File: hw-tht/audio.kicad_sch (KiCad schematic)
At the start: 12 parts, among them U9 PCM5100A

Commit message: hw-tht: v1.3.0, axial/0805 hybrid resistors, decoupling placement
- Board revision v1.3.0 (schematic title blocks and README); take over
  the reviewed layout including the rotated PicoGUS logo and the new
  version and credit texts. The review board is now the build base, so
  its artwork is kept as drawn.
- New R_Axial_DIN0207_P10.16mm_0805_Hybrid footprint (0805 pads between
  the axial holes) for all resistors; BOM lists Yageo RC0805 (DigiKey)
  and UNI-ROYAL 0805W8F (LCSC) alternatives.
- Decoupling back next to the pins it serves, as on v1.2: DAC caps at
  CPVDD/CAPP-CAPM/VNEG/AVDD/DVDD, C4 at U2, C10 at the PSRAM, C3/C5 on
  the supply side of U3/U4. MIDI resistors and ferrites in one row
  next to J5, DAC output filters below the DAC.

Co-Authored-By: Claude Opus 5.5 <noreply@anthropic.com>
Claude-Session: https://claude.ai/code/session_011utN3x8yYUNDvkpGCEq5yD
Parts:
- R7, R8: footprint Resistor_THT:R_Axial_DIN0207_L6.3mm_D2.5mm_P10.16mm_Horizontal -> PicoGUS-THT:R_Axial_DIN0207_P10.16mm_0805_Hybrid; Alternatives (none) -> 0805 SMD (fits between the holes): Yageo RC0805FR-07470RL (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
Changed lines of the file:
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@@
 		(title "PicoGUS THT - PCM510x DAC")
 		(date "2026-09-28")
-		(rev "v1.2-THT")
+		(rev "v1.3.0")
 		(comment 1 "U9 stays SMD (TSSOP-20): PCM5100A/5101A/5102A only exist as SMD")
 	)
@@
 			)
 		)
-		(property "Footprint" "Resistor_THT:R_Axial_DIN0207_L6.3mm_D2.5mm_P10.16mm_Horizontal"
+		(property "Footprint" "PicoGUS-THT:R_Axial_DIN0207_P10.16mm_0805_Hybrid"
 			(at 80.01 48.26 0)
 			(hide yes)
@@
 		)
 		(property "LCSC" "C58592 (UNI-ROYAL MFR0W4F4700A50)"
+			(at 80.01 48.26 0)
+			(hide yes)
+			(effects
+				(font
+					(size 1.27 1.27)
+				)
+				(hide yes)
+			)
+		)
+		(property "Alternatives" "0805 SMD (fits between the holes): Yageo RC0805FR-07470RL (DK 311-470CRCT-ND, 109044), UNI-ROYAL 0805W8F (LCSC C17710, 2072700)."
 			(at 80.01 48.26 0)
 			(hide yes)
@@
 			)
 		)
-		(property "Footprint" "Resistor_THT:R_Axial_DIN0207_L6.3mm_D2.5mm_P10.16mm_Horizontal"
+		(property "Footprint" "PicoGUS-THT:R_Axial_DIN0207_P10.16mm_0805_Hybrid"
 			(at 80.01 45.72 0)
 			(hide yes)
@@
 			(at 80.01 45.72 0)
 			(hide yes)
+			(effects
+				(font
+					(size 1.27 1.27)
+				)
+				(hide yes)
+			)
+		)
+		(property "Alternatives" "0805 SMD (fits between the holes): Yageo RC0805FR-07470RL (DK 311-470CRCT-ND, 109044), UNI-ROYAL 0805W8F (LCSC C17710, 2072700)."
+			(at 80.01 45.72 0)
+			(hide yes)

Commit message: hw-tht: 5 mm disc/0805 hybrid capacitors, labels inside or beside bodies
- New C_Disc_D5.0mm_W2.5mm_P5.00mm_0805_Hybrid footprint for all ceramic
  caps: 5.0/5.08 mm radial part OR an 0805 between the holes. Replaces
  the 2.5/5.0 mm dual-pitch footprint.
- BOM: every ceramic cap line is now 5 mm pitch at both distributors
  (2.2 nF LCSC Dersonic C22391154, 100 pF DigiKey Vishay
  K101J15C0GF5TH5) and lists an in-stock 0805 alternative.
- Silkscreen labels: FB1/FB2 inside the body like the resistors;
  capacitor labels just outside the body, above/left, else at a free end.

Co-Authored-By: Claude Opus 5.5 <noreply@anthropic.com>
Claude-Session: https://claude.ai/code/session_011utN3x8yYUNDvkpGCEq5yD
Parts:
- C12, C13, C14, C18: footprint PicoGUS-THT:C_Disc_D5.0mm_W2.5mm_P2.50mm_P5.00mm -> PicoGUS-THT:C_Disc_D5.0mm_W2.5mm_P5.00mm_0805_Hybrid; Alternatives (none) -> 0805 SMD (fits between the holes): Samsung CL21B104KBCNNNC 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
- C15: footprint PicoGUS-THT:C_Disc_D5.0mm_W2.5mm_P2.50mm_P5.00mm -> PicoGUS-THT:C_Disc_D5.0mm_W2.5mm_P5.00mm_0805_Hybrid; Alternatives (none) -> 0805 SMD 25V X5R: Taiyo Yuden EMK212BJ106KG-T (DK 587-1295-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
- C16, C17: footprint PicoGUS-THT:C_Disc_D5.0mm_W2.5mm_P2.50mm_P5.00mm -> PicoGUS-THT:C_Disc_D5.0mm_W2.5mm_P5.00mm_0805_Hybrid; Alternatives 2.5 mm pitch FG14X7R1H225KRT06 (DK 445-173138-1-ND). -> 0805 SMD: Samsung CL21A225KAFNNNE 25V X5R (DK 1276-1763-1-N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
- C19, C20: footprint PicoGUS-THT:C_Disc_D5.0mm_W2.5mm_P2.50mm_P5.00mm -> PicoGUS-THT:C_Disc_D5.0mm_W2.5mm_P5.00mm_0805_Hybrid; Alternatives KEMET C320C222J1G5TA (DK 399-4281-ND), Vishay K222J15C0GF5T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 -> THT: Vishay K222J15C0GF5TH5 (DK BC1050CT-ND, 1744). 0805 SM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; LCSC C454405 (TORCH CC4-0805-CG-100V-2200pF-J-L (2.54 mm pitch)) -> C22391154 (Dersonic CD1H222JC9PECHD000 (5.08 mm pitch))
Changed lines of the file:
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@@
 			)
 		)
-		(property "Footprint" "PicoGUS-THT:C_Disc_D5.0mm_W2.5mm_P2.50mm_P5.00mm"
+		(property "Footprint" "PicoGUS-THT:C_Disc_D5.0mm_W2.5mm_P5.00mm_0805_Hybrid"
 			(at 90.805 50.8 0)
 			(hide yes)
@@
 			)
 		)
-		(property "LCSC" "C454405 (TORCH CC4-0805-CG-100V-2200pF-J-L (2.54 mm pitch))"
+		(property "LCSC" "C22391154 (Dersonic CD1H222JC9PECHD000 (5.08 mm pitch))"
 			(at 90.805 50.8 0)
 			(hide yes)
@@
 			)
 		)
-		(property "Alternatives" "KEMET C320C222J1G5TA (DK 399-4281-ND), Vishay K222J15C0GF5TL2 (DK BC1029CT-ND)."
+		(property "Alternatives" "THT: Vishay K222J15C0GF5TH5 (DK BC1050CT-ND, 1744). 0805 SMD: Yageo CC0805JRNPO9BN222 (DK 311-1103-1-ND, 126390) / CC0805JKNPO9BN222 (LCSC C107103, 165360)."
 			(at 90.805 50.8 0)
 			(hide yes)
@@
 			)
 		)
-		(property "Footprint" "PicoGUS-THT:C_Disc_D5.0mm_W2.5mm_P2.50mm_P5.00mm"
+		(property "Footprint" "PicoGUS-THT:C_Disc_D5.0mm_W2.5mm_P5.00mm_0805_Hybrid"
 			(at 22.86 47.625 0)
 			(hide yes)
@@
 		)
 		(property "LCSC" "C527620"
+			(at 22.86 47.625 0)
+			(hide yes)
+			(effects
+				(font
+					(size 1.27 1.27)
+				)
+				(hide yes)
+			)
+		)
+		(property "Alternatives" "0805 SMD (fits between the holes): Samsung CL21B104KBCNNNC (DK 1276-1003-1-ND, 4889645; LCSC C1711, 1029920)."
 			(at 22.86 47.625 0)
 			(hide yes)
@@
 			)
 		)
-		(property "Footprint" "PicoGUS-THT:C_Disc_D5.0mm_W2.5mm_P2.50mm_P5.00mm"
+		(property "Footprint" "PicoGUS-THT:C_Disc_D5.0mm_W2.5mm_P5.00mm_0805_Hybrid"
 			(at 80.01 66.04 0)
 			(hide yes)
@@
 		)
 		(property "LCSC" "C527620"
+			(at 80.01 66.04 0)
+			(hide yes)
+			(effects
+				(font
+					(size 1.27 1.27)
+				)
+				(hide yes)
+			)
+		)
+		(property "Alternatives" "0805 SMD (fits between the holes): Samsung CL21B104KBCNNNC (DK 1276-1003-1-ND, 4889645; LCSC C1711, 1029920)."
 			(at 80.01 66.04 0)
 			(hide yes)
@@
 			)
 		)
-		(property "Footprint" "PicoGUS-THT:C_Disc_D5.0mm_W2.5mm_P2.50mm_P5.00mm"
+		(property "Footprint" "PicoGUS-THT:C_Disc_D5.0mm_W2.5mm_P5.00mm_0805_Hybrid"
 			(at 77.47 57.15 0)
 			(hide yes)
@@
 			)
 		)
-		(property "Alternatives" "2.5 mm pitch FG14X7R1H225KRT06 (DK 445-173138-1-ND)."
+		(property "Alternatives" "0805 SMD: Samsung CL21A225KAFNNNE 25V X5R (DK 1276-1763-1-ND, 83806; LCSC C87994, 38740)."
 			(at 77.47 57.15 0)
 			(hide yes)
@@
 			)
 		)
-		(property "Footprint" "PicoGUS-THT:C_Disc_D5.0mm_W2.5mm_P2.50mm_P5.00mm"
+		(property "Footprint" "PicoGUS-THT:C_Disc_D5.0mm_W2.5mm_P5.00mm_0805_Hybrid"
 			(at 90.805 43.18 0)
 			(hide yes)
@@
 			)
 		)
-		(property "LCSC" "C454405 (TORCH CC4-0805-CG-100V-2200pF-J-L (2.54 mm pitch))"
+		(property "LCSC" "C22391154 (Dersonic CD1H222JC9PECHD000 (5.08 mm pitch))"
 			(at 90.805 43.18 0)
 			(hide yes)
@@
 			)
 		)
-		(property "Alternatives" "KEMET C320C222J1G5TA (DK 399-4281-ND), Vishay K222J15C0GF5TL2 (DK BC1029CT-ND)."
+		(property "Alternatives" "THT: Vishay K222J15C0GF5TH5 (DK BC1050CT-ND, 1744). 0805 SMD: Yageo CC0805JRNPO9BN222 (DK 311-1103-1-ND, 126390) / CC0805JKNPO9BN222 (LCSC C107103, 165360)."
 			(at 90.805 43.18 0)
 			(hide yes)
@@
 			)
 		)
-		(property "Footprint" "PicoGUS-THT:C_Disc_D5.0mm_W2.5mm_P2.50mm_P5.00mm"
+		(property "Footprint" "PicoGUS-THT:C_Disc_D5.0mm_W2.5mm_P5.00mm_0805_Hybrid"
 			(at 27.305 47.625 0)
 			(hide yes)
@@
 		)
 		(property "LCSC" "C527620"
+			(at 27.305 47.625 0)
+			(hide yes)
+			(effects
+				(font
+					(size 1.27 1.27)
+				)
+				(hide yes)
+			)
+		)
+		(property "Alternatives" "0805 SMD (fits between the holes): Samsung CL21B104KBCNNNC (DK 1276-1003-1-ND, 4889645; LCSC C1711, 1029920)."
 			(at 27.305 47.625 0)
 			(hide yes)
@@
 			)
 		)
-		(property "Footprint" "PicoGUS-THT:C_Disc_D5.0mm_W2.5mm_P2.50mm_P5.00mm"
+		(property "Footprint" "PicoGUS-THT:C_Disc_D5.0mm_W2.5mm_P5.00mm_0805_Hybrid"
 			(at 36.195 47.625 0)
 			(hide yes)
@@
 		)
 		(property "LCSC" "C3690252"
+			(at 36.195 47.625 0)
+			(hide yes)
+			(effects
+				(font
+					(size 1.27 1.27)
+				)
+				(hide yes)
+			)
+		)
+		(property "Alternatives" "0805 SMD 25V X5R: Taiyo Yuden EMK212BJ106KG-T (DK 587-1295-1-ND, 1864) or Samsung CL21A106KAYNNNE (LCSC C15850, 878060)."
 			(at 36.195 47.625 0)
 			(hide yes)
@@
 			)
 		)
-		(property "Footprint" "PicoGUS-THT:C_Disc_D5.0mm_W2.5mm_P2.50mm_P5.00mm"
+		(property "Footprint" "PicoGUS-THT:C_Disc_D5.0mm_W2.5mm_P5.00mm_0805_Hybrid"
 			(at 77.47 71.12 0)
 			(hide yes)
@@
 			)
 		)
-		(property "Alternatives" "2.5 mm pitch FG14X7R1H225KRT06 (DK 445-173138-1-ND)."
+		(property "Alternatives" "0805 SMD: Samsung CL21A225KAFNNNE 25V X5R (DK 1276-1763-1-ND, 83806; LCSC C87994, 38740)."
 			(at 77.47 71.12 0)
 			(hide yes)
@@
 			)
 		)
-		(property "Footprint" "PicoGUS-THT:C_Disc_D5.0mm_W2.5mm_P2.50mm_P5.00mm"
+		(property "Footprint" "PicoGUS-THT:C_Disc_D5.0mm_W2.5mm_P5.00mm_0805_Hybrid"
 			(at 31.75 47.625 0)
 			(hide yes)
@@
 			(at 31.75 47.625 0)
 			(hide yes)
+			(effects
+				(font
+					(size 1.27 1.27)
+				)
+				(hide yes)
+			)
+		)
+		(property "Alternatives" "0805 SMD (fits between the holes): Samsung CL21B104KBCNNNC (DK 1276-1003-1-ND, 4889645; LCSC C1711, 1029920)."
+			(at 31.75 47.625 0)
+			(hide yes)

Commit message: hw-tht: through-hole parts only, drop the hybrid footprints
- Resistors: plain axial DIN0207 (10.16 mm); ceramic caps: plain 5 mm
  disc; FB1/FB2: axial bead on leads (12.7 mm, Fair-Rite 2743002112 /
  LCSC FH RH3.5x0.8x9P52E); logic ICs: plain DIP-14/DIP-20.
- Only the parts that have no THT version stay SMD: U3/U4 (CB3T3257),
  U8 (APS6404L PSRAM), U9 (PCM510x DAC).
- BOM: 0805/TSSOP alternatives removed. The DIP logic ICs are DigiKey
  parts; LCSC has almost none in stock (listed with their real stock).
- Placement from the latest layout review (DIPs in one column, DAC and
  its caps next to the bus switches), FB1/FB2 and C19/C20 shifted to fit
  the longer bead footprint. Passive labels centred inside the bodies.

Co-Authored-By: Claude Opus 5.5 <noreply@anthropic.com>
Claude-Session: https://claude.ai/code/session_011utN3x8yYUNDvkpGCEq5yD
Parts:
- C12, C13, C14, C18: footprint PicoGUS-THT:C_Disc_D5.0mm_W2.5mm_P5.00mm_0805_Hybrid -> Capacitor_THT:C_Disc_D5.0mm_W2.5mm_P5.00mm; Alternatives 0805 SMD (fits between the holes): Samsung CL21B104KBCNNNC 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 -> (none)
- C15: footprint PicoGUS-THT:C_Disc_D5.0mm_W2.5mm_P5.00mm_0805_Hybrid -> Capacitor_THT:C_Disc_D5.0mm_W2.5mm_P5.00mm; Alternatives 0805 SMD 25V X5R: Taiyo Yuden EMK212BJ106KG-T (DK 587-1295-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 -> (none)
- C16, C17: footprint PicoGUS-THT:C_Disc_D5.0mm_W2.5mm_P5.00mm_0805_Hybrid -> Capacitor_THT:C_Disc_D5.0mm_W2.5mm_P5.00mm; Alternatives 0805 SMD: Samsung CL21A225KAFNNNE 25V X5R (DK 1276-1763-1-N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 -> (none)
- C19, C20: footprint PicoGUS-THT:C_Disc_D5.0mm_W2.5mm_P5.00mm_0805_Hybrid -> Capacitor_THT:C_Disc_D5.0mm_W2.5mm_P5.00mm; Alternatives THT: Vishay K222J15C0GF5TH5 (DK BC1050CT-ND, 1744). 0805 SM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 -> Vishay K222J15C0GF5TH5 (DK BC1050CT-ND, 1744).
- R7, R8: footprint PicoGUS-THT:R_Axial_DIN0207_P10.16mm_0805_Hybrid -> Resistor_THT:R_Axial_DIN0207_L6.3mm_D2.5mm_P10.16mm_Horizontal; Alternatives 0805 SMD (fits between the holes): Yageo RC0805FR-07470RL (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 -> (none)
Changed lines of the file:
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@@
 			)
 		)
-		(property "Footprint" "PicoGUS-THT:C_Disc_D5.0mm_W2.5mm_P5.00mm_0805_Hybrid"
+		(property "Footprint" "Capacitor_THT:C_Disc_D5.0mm_W2.5mm_P5.00mm"
 			(at 90.805 50.8 0)
 			(hide yes)
@@
 			)
 		)
-		(property "Alternatives" "THT: Vishay K222J15C0GF5TH5 (DK BC1050CT-ND, 1744). 0805 SMD: Yageo CC0805JRNPO9BN222 (DK 311-1103-1-ND, 126390) / CC0805JKNPO9BN222 (LCSC C107103, 165360)."
+		(property "Alternatives" "Vishay K222J15C0GF5TH5 (DK BC1050CT-ND, 1744)."
 			(at 90.805 50.8 0)
 			(hide yes)
@@
 			)
 		)
-		(property "Footprint" "PicoGUS-THT:C_Disc_D5.0mm_W2.5mm_P5.00mm_0805_Hybrid"
+		(property "Footprint" "Capacitor_THT:C_Disc_D5.0mm_W2.5mm_P5.00mm"
 			(at 22.86 47.625 0)
 			(hide yes)
@@
 		)
 		(property "LCSC" "C527620"
-			(at 22.86 47.625 0)
-			(hide yes)
-			(effects
-				(font
-					(size 1.27 1.27)
-				)
-				(hide yes)
-			)
-		)
-		(property "Alternatives" "0805 SMD (fits between the holes): Samsung CL21B104KBCNNNC (DK 1276-1003-1-ND, 4889645; LCSC C1711, 1029920)."
 			(at 22.86 47.625 0)
 			(hide yes)
@@
 			)
 		)
-		(property "Footprint" "PicoGUS-THT:C_Disc_D5.0mm_W2.5mm_P5.00mm_0805_Hybrid"
+		(property "Footprint" "Capacitor_THT:C_Disc_D5.0mm_W2.5mm_P5.00mm"
 			(at 80.01 66.04 0)
 			(hide yes)
@@
 		)
 		(property "LCSC" "C527620"
-			(at 80.01 66.04 0)
-			(hide yes)
-			(effects
-				(font
-					(size 1.27 1.27)
-				)
-				(hide yes)
-			)
-		)
-		(property "Alternatives" "0805 SMD (fits between the holes): Samsung CL21B104KBCNNNC (DK 1276-1003-1-ND, 4889645; LCSC C1711, 1029920)."
 			(at 80.01 66.04 0)
 			(hide yes)
@@
 			)
 		)
-		(property "Footprint" "PicoGUS-THT:C_Disc_D5.0mm_W2.5mm_P5.00mm_0805_Hybrid"
+		(property "Footprint" "Capacitor_THT:C_Disc_D5.0mm_W2.5mm_P5.00mm"
 			(at 77.47 57.15 0)
 			(hide yes)
@@
 		)
 		(property "LCSC" "C1623182"
-			(at 77.47 57.15 0)
-			(hide yes)
-			(effects
-				(font
-					(size 1.27 1.27)
-				)
-				(hide yes)
-			)
-		)
-		(property "Alternatives" "0805 SMD: Samsung CL21A225KAFNNNE 25V X5R (DK 1276-1763-1-ND, 83806; LCSC C87994, 38740)."
 			(at 77.47 57.15 0)
 			(hide yes)
@@
 			)
 		)
-		(property "Footprint" "PicoGUS-THT:C_Disc_D5.0mm_W2.5mm_P5.00mm_0805_Hybrid"
+		(property "Footprint" "Capacitor_THT:C_Disc_D5.0mm_W2.5mm_P5.00mm"
 			(at 90.805 43.18 0)
 			(hide yes)
@@
 			)
 		)
-		(property "Alternatives" "THT: Vishay K222J15C0GF5TH5 (DK BC1050CT-ND, 1744). 0805 SMD: Yageo CC0805JRNPO9BN222 (DK 311-1103-1-ND, 126390) / CC0805JKNPO9BN222 (LCSC C107103, 165360)."
+		(property "Alternatives" "Vishay K222J15C0GF5TH5 (DK BC1050CT-ND, 1744)."
 			(at 90.805 43.18 0)
 			(hide yes)
@@
 			)
 		)
-		(property "Footprint" "PicoGUS-THT:C_Disc_D5.0mm_W2.5mm_P5.00mm_0805_Hybrid"
+		(property "Footprint" "Capacitor_THT:C_Disc_D5.0mm_W2.5mm_P5.00mm"
 			(at 27.305 47.625 0)
 			(hide yes)
@@
 		)
 		(property "LCSC" "C527620"
-			(at 27.305 47.625 0)
-			(hide yes)
-			(effects
-				(font
-					(size 1.27 1.27)
-				)
-				(hide yes)
-			)
-		)
-		(property "Alternatives" "0805 SMD (fits between the holes): Samsung CL21B104KBCNNNC (DK 1276-1003-1-ND, 4889645; LCSC C1711, 1029920)."
 			(at 27.305 47.625 0)
 			(hide yes)
@@
 			)
 		)
-		(property "Footprint" "PicoGUS-THT:C_Disc_D5.0mm_W2.5mm_P5.00mm_0805_Hybrid"
+		(property "Footprint" "Capacitor_THT:C_Disc_D5.0mm_W2.5mm_P5.00mm"
 			(at 36.195 47.625 0)
 			(hide yes)
@@
 		)
 		(property "LCSC" "C3690252"
-			(at 36.195 47.625 0)
-			(hide yes)
-			(effects
-				(font
-					(size 1.27 1.27)
-				)
-				(hide yes)
-			)
-		)
-		(property "Alternatives" "0805 SMD 25V X5R: Taiyo Yuden EMK212BJ106KG-T (DK 587-1295-1-ND, 1864) or Samsung CL21A106KAYNNNE (LCSC C15850, 878060)."
 			(at 36.195 47.625 0)
 			(hide yes)
@@
 			)
 		)
-		(property "Footprint" "PicoGUS-THT:C_Disc_D5.0mm_W2.5mm_P5.00mm_0805_Hybrid"
+		(property "Footprint" "Capacitor_THT:C_Disc_D5.0mm_W2.5mm_P5.00mm"
 			(at 77.47 71.12 0)
 			(hide yes)
@@
 		)
 		(property "LCSC" "C1623182"
-			(at 77.47 71.12 0)
-			(hide yes)
-			(effects
-				(font
-					(size 1.27 1.27)
-				)
-				(hide yes)
-			)
-		)
-		(property "Alternatives" "0805 SMD: Samsung CL21A225KAFNNNE 25V X5R (DK 1276-1763-1-ND, 83806; LCSC C87994, 38740)."
 			(at 77.47 71.12 0)
 			(hide yes)
@@
 			)
 		)
-		(property "Footprint" "PicoGUS-THT:R_Axial_DIN0207_P10.16mm_0805_Hybrid"
+		(property "Footprint" "Resistor_THT:R_Axial_DIN0207_L6.3mm_D2.5mm_P10.16mm_Horizontal"
 			(at 80.01 48.26 0)
 			(hide yes)
@@
 		)
 		(property "LCSC" "C58592 (UNI-ROYAL MFR0W4F4700A50)"
-			(at 80.01 48.26 0)
-			(hide yes)
-			(effects
-				(font
-					(size 1.27 1.27)
-				)
-				(hide yes)
-			)
-		)
-		(property "Alternatives" "0805 SMD (fits between the holes): Yageo RC0805FR-07470RL (DK 311-470CRCT-ND, 109044), UNI-ROYAL 0805W8F (LCSC C17710, 2072700)."
 			(at 80.01 48.26 0)
 			(hide yes)
@@
 			)
 		)
-		(property "Footprint" "PicoGUS-THT:C_Disc_D5.0mm_W2.5mm_P5.00mm_0805_Hybrid"
+		(property "Footprint" "Capacitor_THT:C_Disc_D5.0mm_W2.5mm_P5.00mm"
 			(at 31.75 47.625 0)
 			(hide yes)
@@
 		)
 		(property "LCSC" "C527620"
-			(at 31.75 47.625 0)
-			(hide yes)
-			(effects
-				(font
-					(size 1.27 1.27)
-				)
-				(hide yes)
-			)
-		)
-		(property "Alternatives" "0805 SMD (fits between the holes): Samsung CL21B104KBCNNNC (DK 1276-1003-1-ND, 4889645; LCSC C1711, 1029920)."
 			(at 31.75 47.625 0)
 			(hide yes)
@@
 			)
 		)
-		(property "Footprint" "PicoGUS-THT:R_Axial_DIN0207_P10.16mm_0805_Hybrid"
+		(property "Footprint" "Resistor_THT:R_Axial_DIN0207_L6.3mm_D2.5mm_P10.16mm_Horizontal"
 			(at 80.01 45.72 0)
 			(hide yes)
@@
 			(at 80.01 45.72 0)
 			(hide yes)
-			(effects
-				(font
-					(size 1.27 1.27)
-				)
-				(hide yes)
-			)
-		)
-		(property "Alternatives" "0805 SMD (fits between the holes): Yageo RC0805FR-07470RL (DK 311-470CRCT-ND, 109044), UNI-ROYAL 0805W8F (LCSC C17710, 2072700)."
-			(at 80.01 45.72 0)
-			(hide yes)

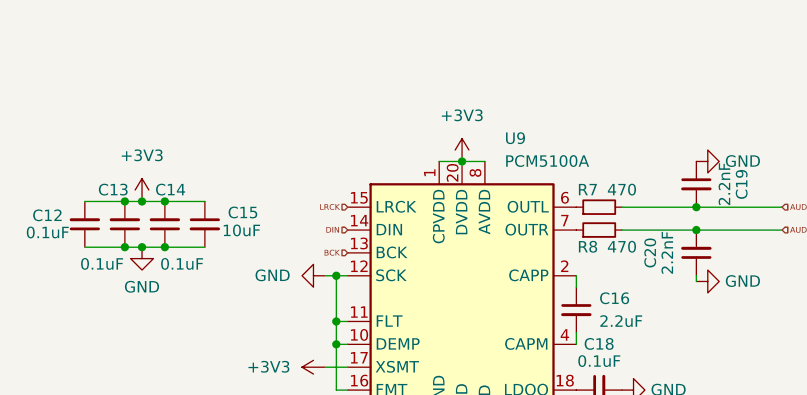
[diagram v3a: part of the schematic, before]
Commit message: hw-tht: cleaner audio supplies, bipolar WT coupling caps, circuit-block groups
- DAC AVDD (U9 pin 8) gets its own rail behind ferrite bead FB3, with C13/C15
  at the pin; DVDD/CPVDD stay on the Pico 3V3.
- NE5532 +/-12 V from ISA through R23/R24 (10R) + C32/C33 (47uF) RC filters,
  C28/C29 0.1uF stay at the op-amp pins.
- C22/C23 WT coupling caps are now 10uF bipolar (Panasonic ECE-A1HN100U):
  the DC across them depends on the daughterboard.
- Every chip and its decoupling caps/resistors form a KiCad group.
- DAC pre-routes reworked (VNEG via B.Cu, XSMT via); RUN RC moved out of the
  Pico fan-in. Fully routed, 0 DRC errors, 0 unconnected.
- BOM: new lines for R23/R24, FB3, C32/C33; README has DigiKey cost in NOK.

Co-Authored-By: Claude Opus 5.5 <noreply@anthropic.com>
Claude-Session: https://claude.ai/code/session_011utN3x8yYUNDvkpGCEq5yD
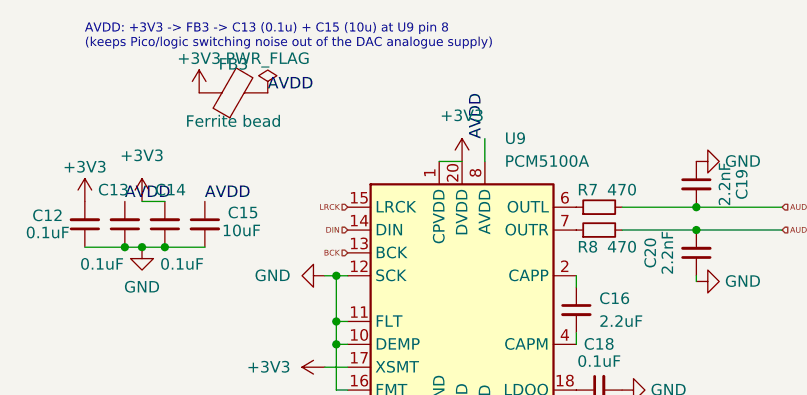
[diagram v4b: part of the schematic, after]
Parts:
- added FB3: Ferrite bead, Resistor_THT:R_Axial_DIN0309_L9.0mm_D3.2mm_P12.70mm_Horizontal, symbol Device:FerriteBead
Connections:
- net +3V3: now also FB3.1; no longer C13.2, C15.1, U9.8 (AVDD)
- new net AVDD: C13.2, C15.1, FB3.2, U9.8 (AVDD)
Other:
- note added: "AVDD: +3V3 -> FB3 -> C13 (0.1u) + C15 (10u) at U9 pin 8 (keeps Pico/logic switching noise out of the DAC analogue supply)"
